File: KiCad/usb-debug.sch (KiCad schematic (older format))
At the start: 77 parts, among them IC15 TLV70018DCKT, IC16 AP22652W6-7, IC7 HD3SS3220, J11 632723300011, Q1 PMV32UP, T6 BSS138APW, T7 BSS138APW

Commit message: Move ethernet connector closet to the edge. Loclib
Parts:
- removed D6, D7: ~, jetson-nano-baseboard-footprints:TPD4E05U06_PASS, symbol jetson-nano-baseboard:TPD4E05U06
- added D6, D7: TPD4E05U06_PASS, jetson-nano-baseboard-footprints:TPD4E05U06_PASS, symbol jetson-nano-baseboard:TPD4E05U06_PASS
- C32: footprint antmicro-footprints:0402-cap -> jetson-nano-baseboard-footprints:0402-cap; symbol antmicroCapacitors0402:C_10u_0402 -> jetson-nano-baseboard:C_10u_0402
- D3, D5, D8, D9: footprint antmicro-footprints:SOT-23s -> jetson-nano-baseboard-footprints:SOT-23s; symbol antmicroTVSDiodes:PESD2USB5UV-TR -> jetson-nano-baseboard:PESD2USB5UV-TR
- IC16: footprint antmicro-footprints:SOT-23-6 -> jetson-nano-baseboard-footprints:SOT-23-6; symbol antmicroPMICPowerDistributionSwitchesLoadDrivers:AP22652W6-7 -> jetson-nano-baseboard:AP22652W6-7
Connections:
- net labels removed: TPD4E05U06DQAR
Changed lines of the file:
@@
 Text Label 600  10175 0    60   ~ 0
 USBC_ID
-Text Label 12600 5075 1    70   ~ 0
-TPD4E05U06DQAR
 Text Label 11075 4675 0    60   ~ 0
 C_USBSS_TX1_P
@@
 Text Label 11075 4475 0    60   ~ 0
 C_USBSS_RX1_N
-Text Label 14400 5075 1    70   ~ 0
-TPD4E05U06DQAR
 Text Label 10525 2725 0    60   ~ 0
 C_CC1
@@
 $EndComp
 $Comp
-L jetson-nano-baseboard:TPD4E05U06 D6
-U 1 1 5E710322
-P 12075 4675
-F 0 "D6" H 12075 4975 60  0000 L BNN
-F 1 "~" H 12075 4675 50  0001 C CNN
-F 2 "jetson-nano-baseboard-footprints:TPD4E05U06_PASS" H 12075 4675 50  0001 C CNN
-F 3 "" H 12075 4675 50  0001 C CNN
-F 4 "Texas Instruments" V 775 -2518 60  0001 C CNN "Manufacturer"
-F 5 "TPD4E05U06DQAR" V 775 -2518 60  0001 C CNN "PartSymbol"
-F 6 "TPD4E05U06DQAR" H -31496 -14030 50  0001 C CNN "MPN"
-	1    12075 4675
-	1    0    0    -1
-$EndComp
-$Comp
-L jetson-nano-baseboard:TPD4E05U06 D7
-U 1 1 5E710321
-P 13850 4675
-F 0 "D7" H 13850 4975 60  0000 L BNN
-F 1 "~" H 13850 4675 50  0001 C CNN
-F 2 "jetson-nano-baseboard-footprints:TPD4E05U06_PASS" H 13850 4675 50  0001 C CNN
-F 3 "" H 13850 4675 50  0001 C CNN
-F 4 "Texas Instruments" V 750 -2518 60  0001 C CNN "Manufacturer"
-F 5 "TPD4E05U06DQAR" V 750 -2518 60  0001 C CNN "PartSymbol"
-F 6 "TPD4E05U06DQAR" H -31521 -14030 50  0001 C CNN "MPN"
-	1    13850 4675
-	1    0    0    -1
-$EndComp
-$Comp
 L jetson-nano-baseboard:BLM18SG121TN1D L7
 U 1 1 5E71031F
@@
 $EndComp
 $Comp
-L antmicroPMICPowerDistributionSwitchesLoadDrivers:AP22652W6-7 IC16
+L jetson-nano-baseboard:AP22652W6-7 IC16
 U 1 1 618DCEF2
 P 4325 9475
 F 0 "IC16" H 4075 9150 50  0000 C CNN
 F 1 "AP22652W6-7" H 4275 9225 50  0000 C CNN
-F 2 "antmicro-footprints:SOT-23-6" H 4325 9225 50  0001 C CNN
+F 2 "jetson-nano-baseboard-footprints:SOT-23-6" H 4325 9225 50  0001 C CNN
 F 3 "https://www.diodes.com/assets/Datasheets/AP22652_53_52A_53A.pdf" H 4325 9475 50  0001 C CNN
 F 4 "Diodes Incorporated " H 4325 9125 50  0001 C CNN "Manufacturer"
@@
 	4725 9575 5000 9575
 $Comp
-L antmicroCapacitors0402:C_10u_0402 C32
+L jetson-nano-baseboard:C_10u_0402 C32
 U 1 1 619B98FA
 P 3425 9775
 F 0 "C32" H 3540 9820 60  0000 L CNN
 F 1 "C_10u_0402" H 3425 9625 60  0001 C CNN
-F 2 "antmicro-footprints:0402-cap" H 3625 9975 60  0001 L CNN
+F 2 "jetson-nano-baseboard-footprints:0402-cap" H 3625 9975 60  0001 L CNN
 F 3 "" H 3425 9775 50  0001 C CNN
 F 4 "MURATA" H 3625 10175 60  0001 L CNN "Manufacturer"
@@
 $EndComp
 $Comp
-L antmicroTVSDiodes:PESD2USB5UV-TR D9
+L jetson-nano-baseboard:PESD2USB5UV-TR D9
 U 1 1 61BF6079
 P 6625 6700
 F 0 "D9" V 7108 6600 60  0000 C CNN
 F 1 "PESD2USB5UV-TR" V 7214 6600 60  0000 C CNN
-F 2 "antmicro-footprints:SOT-23s" H 6675 6900 60  0001 C CNN
+F 2 "jetson-nano-baseboard-footprints:SOT-23s" H 6675 6900 60  0001 C CNN
 F 3 "https://assets.nexperia.com/documents/data-sheet/PESD2USB5UV-T.pdf" H 6625 6700 60  0001 C CNN
 F 4 "PESD2USB5UV-TR " H 6325 7000 50  0001 C CNN "MPN"
@@
 $EndComp
 $Comp
-L antmicroTVSDiodes:PESD2USB5UV-TR D8
+L jetson-nano-baseboard:PESD2USB5UV-TR D8
 U 1 1 61BFA215
 P 8025 6700
 F 0 "D8" V 8508 6600 60  0000 C CNN
 F 1 "PESD2USB5UV-TR" V 8614 6600 60  0000 C CNN
-F 2 "antmicro-footprints:SOT-23s" H 8075 6900 60  0001 C CNN
+F 2 "jetson-nano-baseboard-footprints:SOT-23s" H 8075 6900 60  0001 C CNN
 F 3 "https://assets.nexperia.com/documents/data-sheet/PESD2USB5UV-T.pdf" H 8025 6700 60  0001 C CNN
 F 4 "PESD2USB5UV-TR " H 7725 7000 50  0001 C CNN "MPN"
@@
 $EndComp
 $Comp
-L antmicroTVSDiodes:PESD2USB5UV-TR D5
+L jetson-nano-baseboard:PESD2USB5UV-TR D5
 U 1 1 61C529C6
 P 10425 4475
 F 0 "D5" H 10518 4764 60  0000 C CNN
 F 1 "PESD2USB5UV-TR" H 10518 4658 60  0000 C CNN
-F 2 "antmicro-footprints:SOT-23s" H 10475 4675 60  0001 C CNN
+F 2 "jetson-nano-baseboard-footprints:SOT-23s" H 10475 4675 60  0001 C CNN
 F 3 "https://assets.nexperia.com/documents/data-sheet/PESD2USB5UV-T.pdf" H 10425 4475 60  0001 C CNN
 F 4 "PESD2USB5UV-TR " H 10125 4775 50  0001 C CNN "MPN"
@@
 $EndComp
 $Comp
-L antmicroTVSDiodes:PESD2USB5UV-TR D3
+L jetson-nano-baseboard:PESD2USB5UV-TR D3
 U 1 1 61C696B4
 P 13375 7325
 F 0 "D3" V 13858 7225 60  0000 C CNN
 F 1 "PESD2USB5UV-TR" V 13964 7225 60  0000 C CNN
-F 2 "antmicro-footprints:SOT-23s" H 13425 7525 60  0001 C CNN
+F 2 "jetson-nano-baseboard-footprints:SOT-23s" H 13425 7525 60  0001 C CNN
 F 3 "https://assets.nexperia.com/documents/data-sheet/PESD2USB5UV-T.pdf" H 13375 7325 60  0001 C CNN
 F 4 "PESD2USB5UV-TR " H 13075 7625 50  0001 C CNN "MPN"
@@
 	0    1    1    0
 $EndComp
+$Comp
+L jetson-nano-baseboard:TPD4E05U06_PASS D6
+U 1 1 63492E55
+P 12075 4675
+F 0 "D6" H 12168 5164 60  0000 C CNN
+F 1 "TPD4E05U06_PASS" H 12168 5058 60  0000 C CNN
+F 2 "jetson-nano-baseboard-footprints:TPD4E05U06_PASS" H 12075 4675 60  0001 C CNN
+F 3 "" H 12075 4675 60  0001 C CNN
+F 4 "Texas Instruments" H 12075 4675 50  0001 C CNN "Manufacturer"
+F 5 "TPD4E05U06DQAR" H 12075 4675 50  0001 C CNN "MPN"
+	1    12075 4675
+	1    0    0    -1
+$EndComp
+$Comp
+L jetson-nano-baseboard:TPD4E05U06_PASS D7
+U 1 1 634A34A2
+P 13850 4675
+F 0 "D7" H 14280 4678 60  0000 L CNN
+F 1 "TPD4E05U06_PASS" H 14280 4572 60  0000 L CNN
+F 2 "jetson-nano-baseboard-footprints:TPD4E05U06_PASS" H 13850 4675 60  0001 C CNN
+F 3 "" H 13850 4675 60  0001 C CNN
+F 4 "Texas Instruments" H 13850 4675 50  0001 C CNN "Manufacturer"
+F 5 "TPD4E05U06DQAR" H 13850 4675 50  0001 C CNN "MPN"
+	1    13850 4675
+	1    0    0    -1
+$EndComp
 $EndSCHEMATC

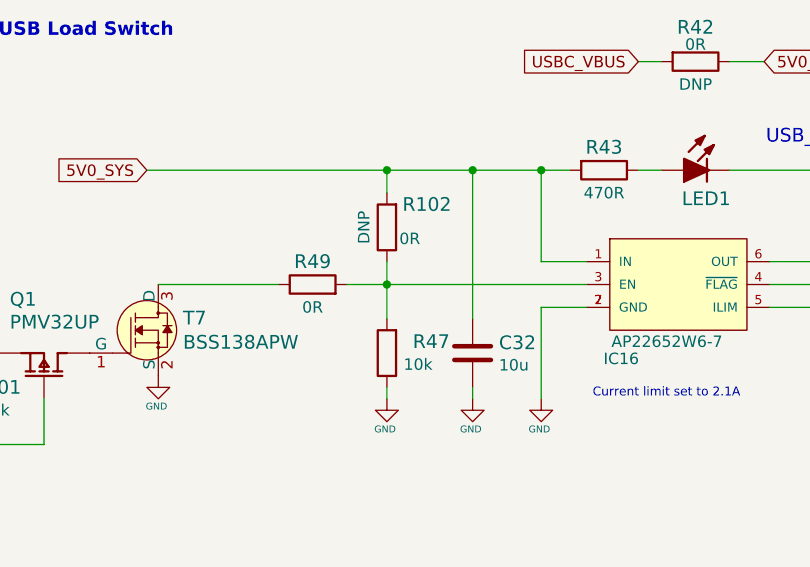
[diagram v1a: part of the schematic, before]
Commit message: Replace ethernet connector, fix traces and tuning
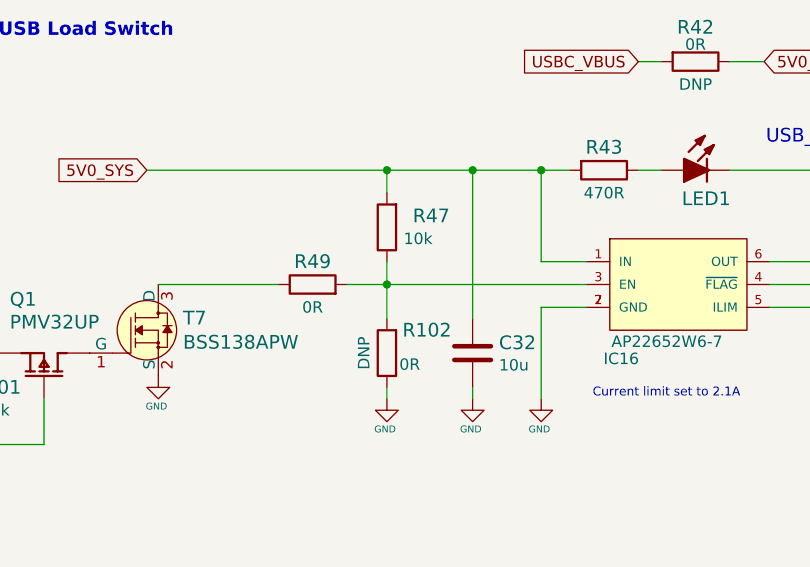
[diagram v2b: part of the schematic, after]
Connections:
- net 5V0_SYS: now also R47.2; no longer R102.2
- net GND: now also R102.1; no longer R47.1
- net at IC16.3 (EN), R49.2: now also R102.2, R47.1; no longer R102.1, R47.2
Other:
- moved on the sheet: R102, R47
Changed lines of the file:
@@
 L jetson-nano-baseboard:R_10k_0402 R47
 U 1 1 62A1B644
-P 3050 9775
-F 0 "R47" V 3100 9500 60  0000 L CNN
-F 1 "R_10k_0402" H 3050 9625 60  0001 C CNN
-F 2 "jetson-nano-baseboard-footprints:0402-res" H 3250 9975 60  0001 L CNN
-F 3 "" H 3050 9775 50  0001 C CNN
-F 4 "VISHAY" H 3250 10175 60  0001 L CNN "Manufacturer"
-F 5 "CRCW040210K0FKEDHP" H 3250 10075 60  0001 L CNN "MPN"
-F 6 "10k" V 3000 9575 50  0000 L CNN "Val"
-	1    3050 9775
+P 3050 9225
+F 0 "R47" V 3100 8950 60  0000 L CNN
+F 1 "R_10k_0402" H 3050 9075 60  0001 C CNN
+F 2 "jetson-nano-baseboard-footprints:0402-res" H 3250 9425 60  0001 L CNN
+F 3 "" H 3050 9225 50  0001 C CNN
+F 4 "VISHAY" H 3250 9625 60  0001 L CNN "Manufacturer"
+F 5 "CRCW040210K0FKEDHP" H 3250 9525 60  0001 L CNN "MPN"
+F 6 "10k" V 3000 9025 50  0000 L CNN "Val"
+	1    3050 9225
 	0    -1   -1   0
 $EndComp
@@
 L jetson-nano-baseboard:R_0R_0402 R102
 U 1 1 62A9631F
-P 3050 9225
-F 0 "R102" V 3150 9050 60  0000 C CNN
-F 1 "R_0R_0402" H 3050 9075 60  0001 C CNN
-F 2 "jetson-nano-baseboard-footprints:0402-res" H 3250 9425 60  0001 L CNN
-F 3 "" H 3050 9225 50  0001 C CNN
-F 4 "PANASONIC" H 3250 9625 60  0001 L CNN "Manufacturer"
-F 5 "ERJ2GE0R00X" H 3250 9525 60  0001 L CNN "MPN"
-F 6 "0R" V 3000 9125 50  0000 C CNN "Val"
-F 7 "DNP" H 3050 9325 50  0000 C CNN "DNP"
-	1    3050 9225
+P 3050 9775
+F 0 "R102" V 3150 9600 60  0000 C CNN
+F 1 "R_0R_0402" H 3050 9625 60  0001 C CNN
+F 2 "jetson-nano-baseboard-footprints:0402-res" H 3250 9975 60  0001 L CNN
+F 3 "" H 3050 9775 50  0001 C CNN
+F 4 "PANASONIC" H 3250 10175 60  0001 L CNN "Manufacturer"
+F 5 "ERJ2GE0R00X" H 3250 10075 60  0001 L CNN "MPN"
+F 6 "0R" V 3000 9675 50  0000 C CNN "Val"
+F 7 "DNP" H 3050 9875 50  0000 C CNN "DNP"
+	1    3050 9775
 	0    -1   -1   0
 $EndComp
